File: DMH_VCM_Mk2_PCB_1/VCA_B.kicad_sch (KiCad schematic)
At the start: 19 parts, among them Q3 BC548, Q4 BC548, U1 TL074

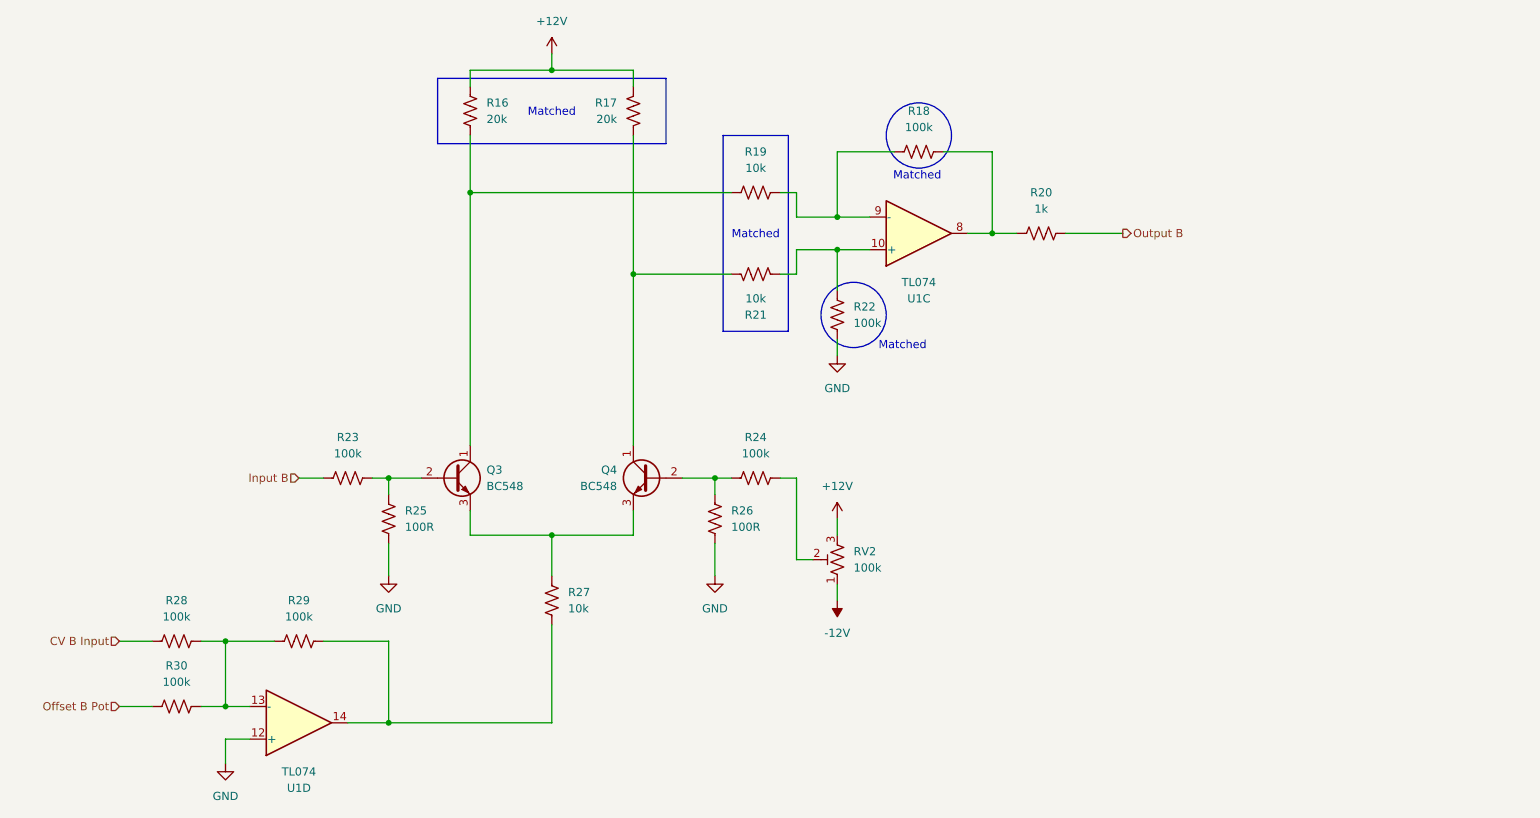
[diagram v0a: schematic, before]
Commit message: Almost finished PCB 1 schematic
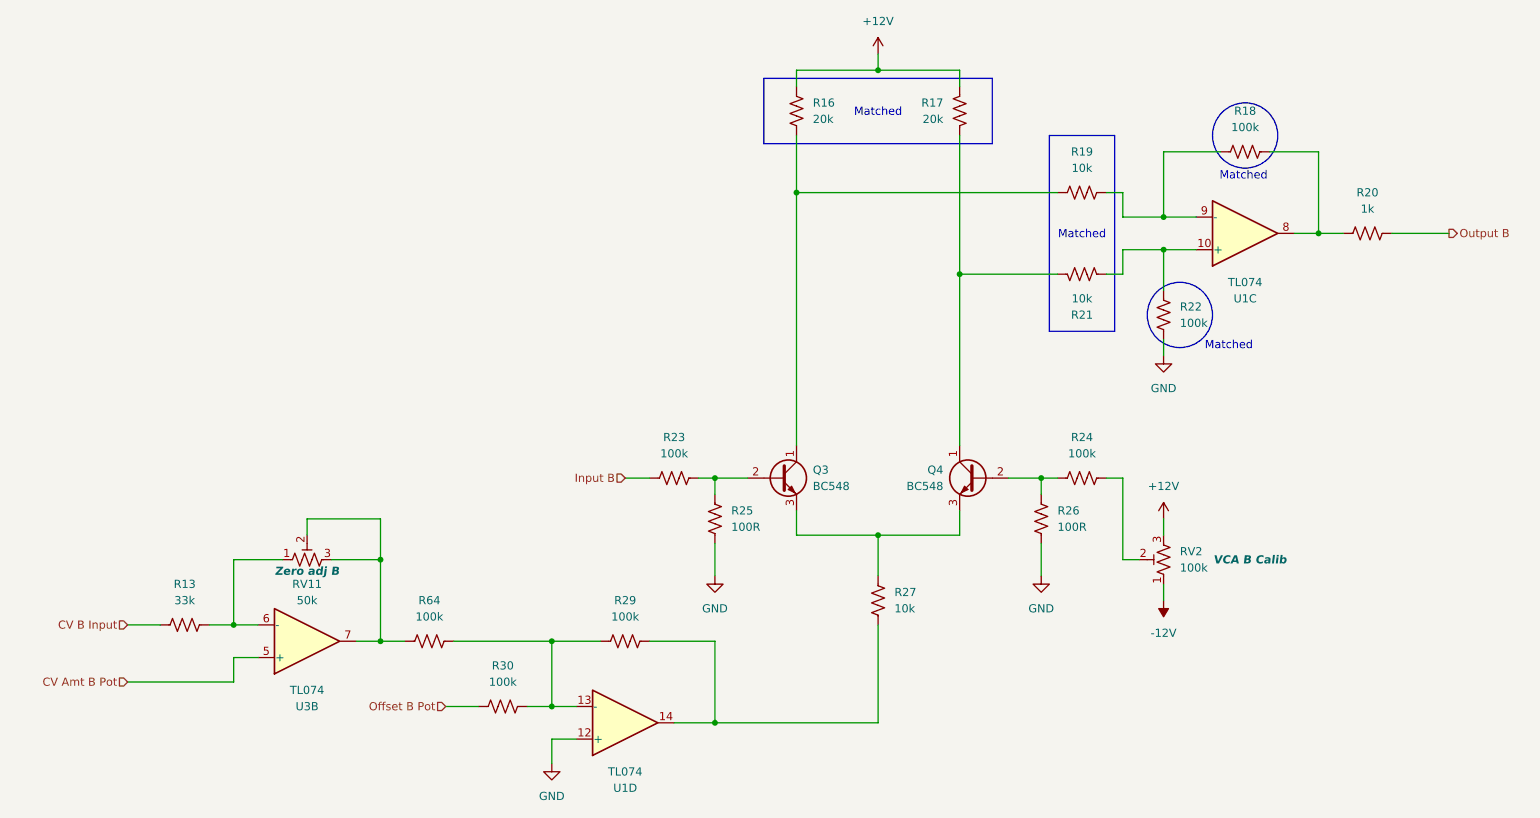
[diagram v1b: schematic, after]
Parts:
- removed R28: 100k, Resistor_THT:R_Axial_DIN0207_L6.3mm_D2.5mm_P2.54mm_Vertical, symbol Device:R_US
- added R13: 33k, Resistor_THT:R_Axial_DIN0207_L6.3mm_D2.5mm_P7.62mm_Horizontal, symbol Device:R_US
- added R64: 100k, Resistor_THT:R_Axial_DIN0207_L6.3mm_D2.5mm_P7.62mm_Horizontal, symbol Device:R_US
- added RV11: 50k, Potentiometer_THT:Potentiometer_Bourns_3296W_Vertical, symbol Device:R_Potentiometer_Trim_US
- added U3: TL074, Package_DIP:DIP-14_W7.62mm_Socket, symbol Amplifier_Operational:TL074
- RV2: Function (none) -> VCA B Calib
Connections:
- net CV B Input: now also R13.1
- net at R29.1, R30.2, U1.13 (-): now also R64.2
- new net: R64.1, RV11.2, RV11.3, U3.7
- new net: R13.2, RV11.1, U3.6 (-)
- new net CV Amt B Pot: U3.5 (+)
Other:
- moved on the sheet: Q3, Q4, R16, R17, R18, R19, R20, R21, R22, R23, R24, R25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

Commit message: PCB 1 placement in progress
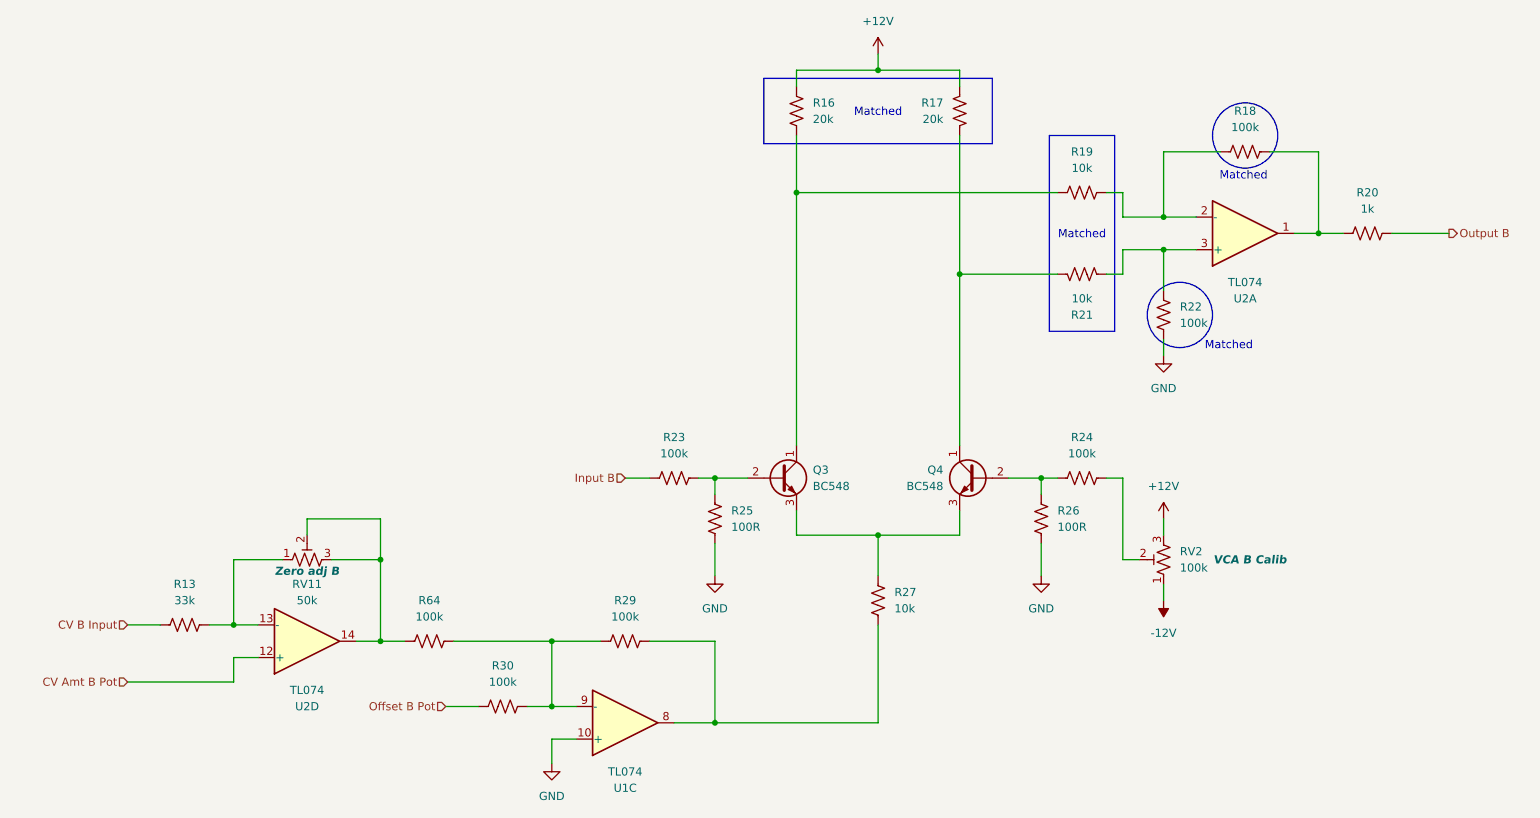
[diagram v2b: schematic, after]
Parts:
- R13, R64: footprint Resistor_THT:R_Axial_DIN0207_L6.3mm_D2.5mm_P7.62mm_Horizontal -> Resistor_THT:R_Axial_DIN0207_L6.3mm_D2.5mm_P2.54mm_Vertical
- renumbered U1 to U2, U3 to U2
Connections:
- net CV Amt B Pot: now also U2.12 (+); no longer U2.5 (+)
- net GND: now also U1.10 (+); no longer U1.12 (+)
- net at R18.1, R20.2: now also U2.1; no longer U2.8
- net at R18.2, R19.1: now also U2.2 (-); no longer U2.9 (-)
- net at R64.1, RV11.2, RV11.3: now also U2.14; no longer U2.7
- net at R29.1, R30.2, R64.2: now also U1.9 (-); no longer U1.13 (-)
- net at R21.1, R22.1: now also U2.3 (+); no longer U2.10 (+)
- net at R13.2, RV11.1: now also U2.13 (-); no longer U2.6 (-)
- net at R27.1, R29.2: now also U1.8; no longer U1.14
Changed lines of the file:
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@@
 			)
 		)
-		(property "Footprint" "Resistor_THT:R_Axial_DIN0207_L6.3mm_D2.5mm_P7.62mm_Horizontal"
+		(property "Footprint" "Resistor_THT:R_Axial_DIN0207_L6.3mm_D2.5mm_P2.54mm_Vertical"
 			(at 108.204 138.684 90)
 			(effects
@@
 		(at 234.95 76.2 0)
 		(mirror x)
-		(unit 3)
-		(exclude_from_sim no)
-		(in_bom yes)
-		(on_board yes)
-		(dnp no)
-		(property "Reference" "U1"
+		(unit 1)
+		(exclude_from_sim no)
+		(in_bom yes)
+		(on_board yes)
+		(dnp no)
+		(property "Reference" "U2"
 			(at 234.95 86.36 0)
 			(effects
@@
 			(project "DMH_Tripple_VCA_PCB_1"
 				(path "/58f4306d-5387-4983-bb08-41a2313fd315/b1c4e848-8fe8-4310-abec-b04b02b54b3f"
-					(reference "U1")
-					(unit 3)
+					(reference "U2")
+					(unit 1)
 				)
 			)
@@
 			)
 		)
-		(property "Footprint" "Resistor_THT:R_Axial_DIN0207_L6.3mm_D2.5mm_P7.62mm_Horizontal"
+		(property "Footprint" "Resistor_THT:R_Axial_DIN0207_L6.3mm_D2.5mm_P2.54mm_Vertical"
 			(at 70.104 136.144 90)
 			(effects
@@
 		(at 138.43 152.4 0)
 		(mirror x)
-		(unit 4)
+		(unit 3)
 		(exclude_from_sim no)
 		(in_bom yes)
@@
 				(path "/58f4306d-5387-4983-bb08-41a2313fd315/b1c4e848-8fe8-4310-abec-b04b02b54b3f"
 					(reference "U1")
-					(unit 4)
+					(unit 3)
 				)
 			)
@@
 		(at 88.9 139.7 0)
 		(mirror x)
-		(unit 2)
-		(exclude_from_sim no)
-		(in_bom yes)
-		(on_board yes)
-		(dnp no)
-		(property "Reference" "U3"
+		(unit 4)
+		(exclude_from_sim no)
+		(in_bom yes)
+		(on_board yes)
+		(dnp no)
+		(property "Reference" "U2"
 			(at 88.9 149.86 0)
 			(effects
@@
 			(project "DMH_VCM_Mk2_PCB_1"
 				(path "/58f4306d-5387-4983-bb08-41a2313fd315/b1c4e848-8fe8-4310-abec-b04b02b54b3f"
-					(reference "U3")
-					(unit 2)
-				)
-			)
+					(reference "U2")
+					(unit 4)
+				)
+			)

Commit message: PCB 1 placement done
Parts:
- RV2: Function VCA B Calib -> Calib B
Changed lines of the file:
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@@
 			)
 		)
-		(property "Function" "VCA B Calib"
-			(at 235.712 127 0)
+		(property "Function" "Calib B"
+			(at 233.172 127 0)
 			(effects
 				(font
